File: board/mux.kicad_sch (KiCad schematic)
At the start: 2 parts, among them U1 ADG707BRUZ-REEL7

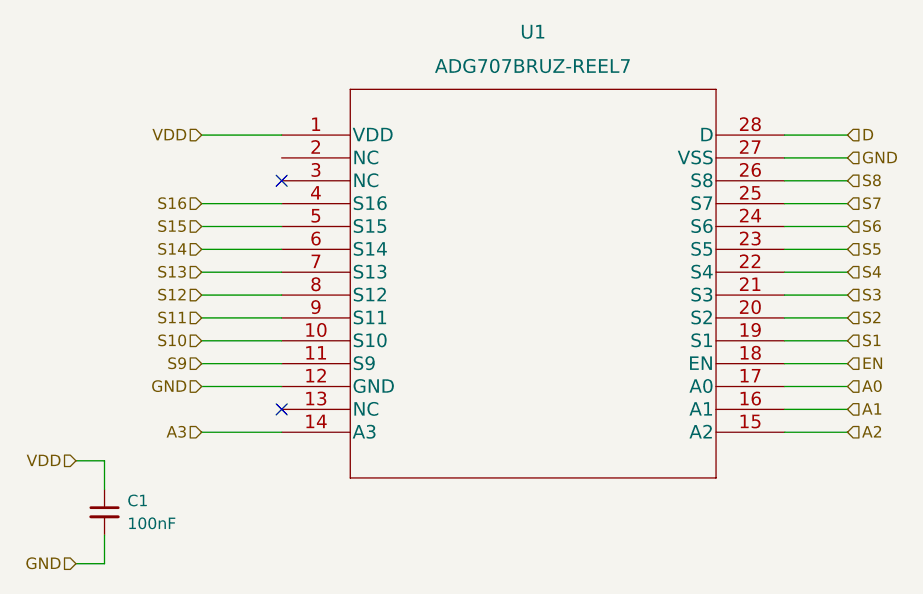
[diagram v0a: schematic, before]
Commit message: fixed part number and added 3D model
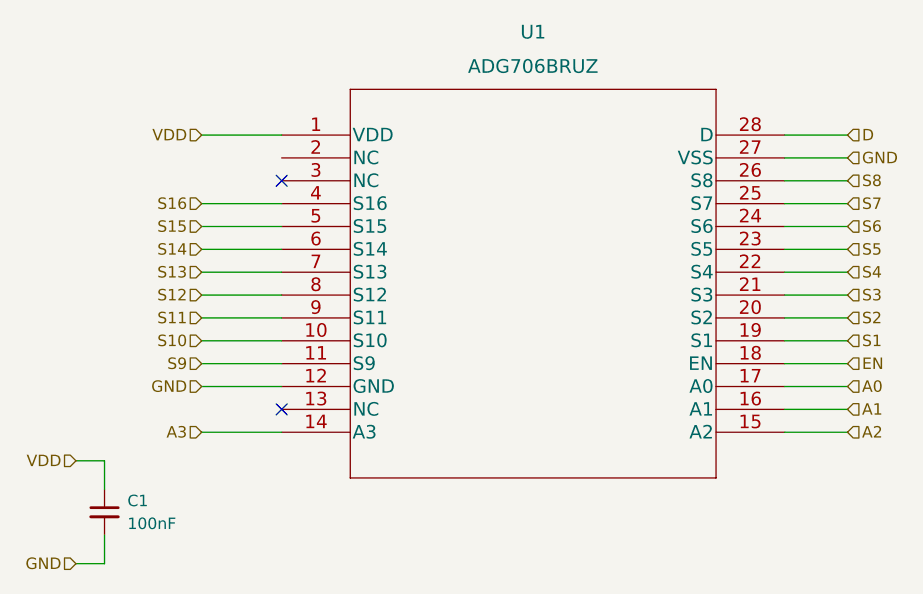
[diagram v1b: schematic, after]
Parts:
- U1: value ADG707BRUZ-REEL7 -> ADG706BRUZ; footprint b112:ADG707BRUZ-REEL7 -> b112:ADG706BRUZ-REEL7
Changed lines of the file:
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@@
       (effects (font (size 1.524 1.524)))
     )
-    (property "Value" "ADG707BRUZ-REEL7" (id 1) (at 149.225 71.12 0)
+    (property "Value" "ADG706BRUZ" (id 1) (at 149.225 71.12 0)
       (effects (font (size 1.524 1.524)))
     )
-    (property "Footprint" "b112:ADG707BRUZ-REEL7" (id 2) (at 149.225 72.644 0)
+    (property "Footprint" "b112:ADG706BRUZ-REEL7" (id 2) (at 149.225 72.644 0)
       (effects (font (size 1.524 1.524)) hide)
     )
